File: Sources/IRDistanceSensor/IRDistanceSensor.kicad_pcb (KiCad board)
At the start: 2 copper layers, 31 x 22 mm, 2 parts

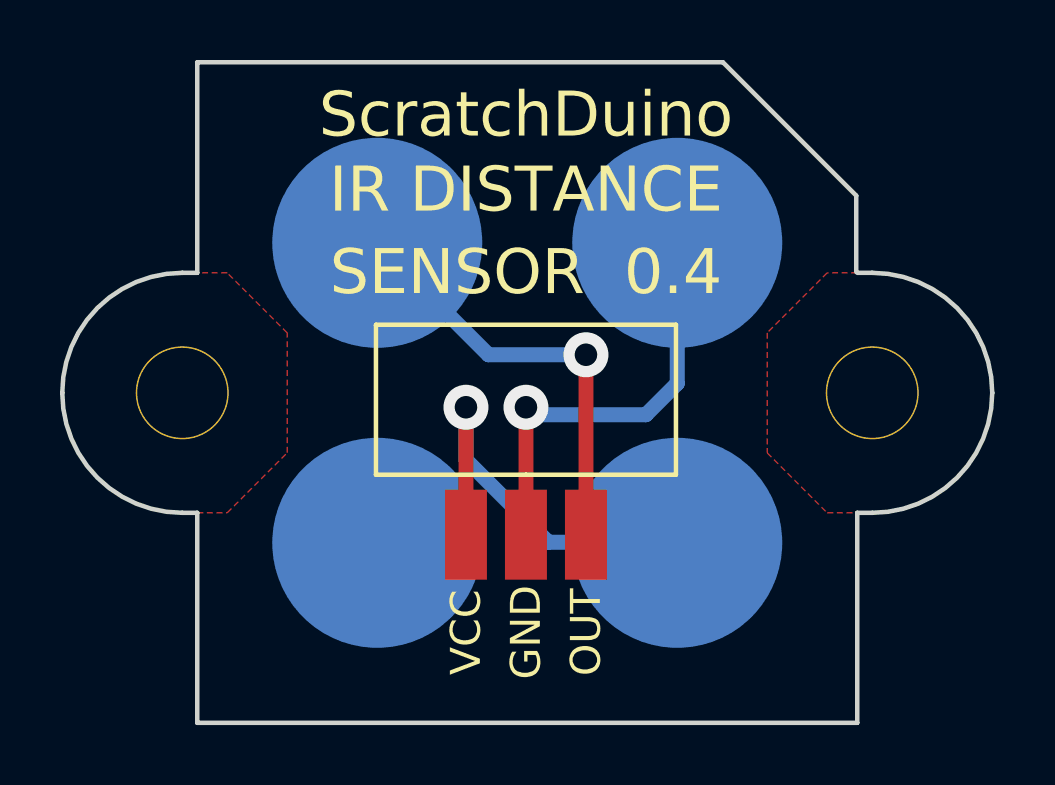
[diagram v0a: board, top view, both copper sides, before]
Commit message: new IR Distance Sensor
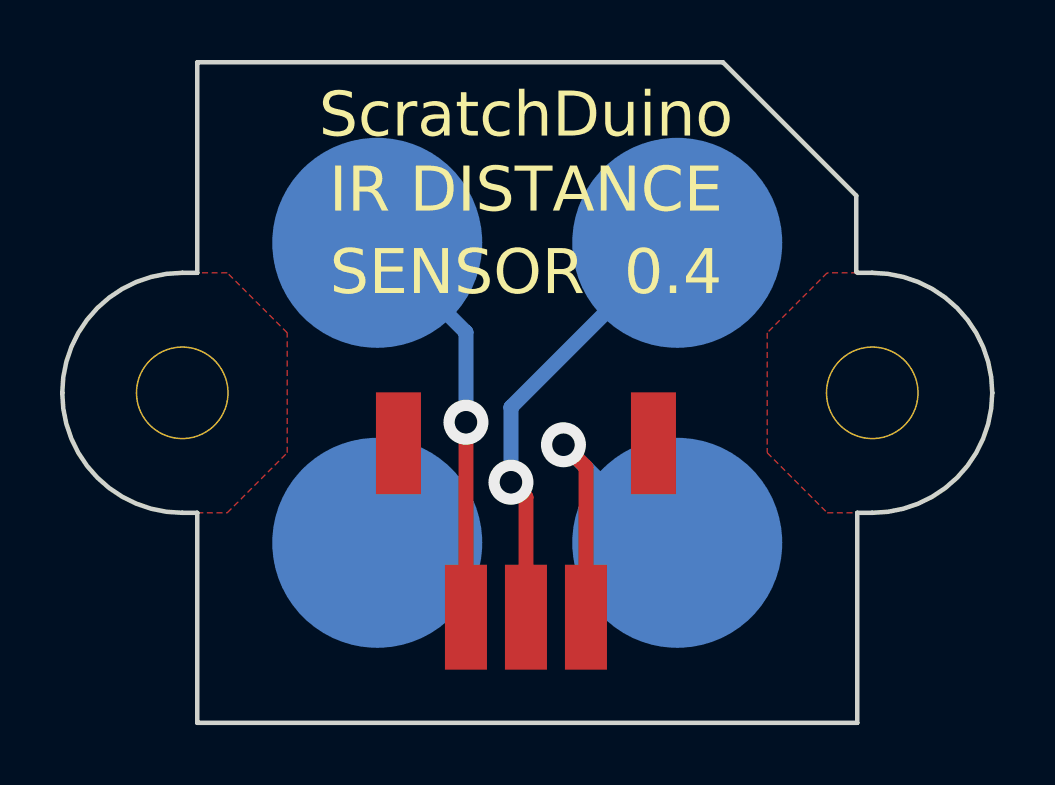
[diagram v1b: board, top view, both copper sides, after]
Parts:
- moved ? 2.75 mm to (29.2, 50.2)
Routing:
- net N-000002: track 14.2 -> 11.2 mm
- net N-000004: track 14.5 -> 13.7 mm
- net N-000003: track 14.5 -> 15.0 mm
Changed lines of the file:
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@@
     (links 3)
     (no_connects 0)
-    (area 13.488999 31.464999 59.829 60.829)
+    (area 13.488999 31.464999 59.829 63.579)
     (thickness 1.6)
     (drawings 18)
-    (tracks 17)
+    (tracks 16)
     (zones 0)
     (modules 2)
@@
     (mod_text_size 1.5 1.5)
     (mod_text_width 0.15)
-    (pad_size 1.4 3)
+    (pad_size 1.5 3.4)
     (pad_drill 0)
     (pad_to_mask_clearance 0.2)
@@
   )
   (module IRDISTANCEWIRE (layer F.Cu)
-    (at 29.25 47.5)
+    (at 29.25 50.25)
     (fp_text reference "" (at 23.5 12.25) (layer F.SilkS)
       (effects (font (size 1.5 1.5) (thickness 0.15)))
@@
       (effects (font (size 1.5 1.5) (thickness 0.15)))
     )
-    (fp_line (start -5 -2) (end -5 -7) (layer F.SilkS) (width 0.15))
-    (fp_line (start -5 -7) (end 5 -7) (layer F.SilkS) (width 0.15))
-    (fp_line (start 5 -7) (end 5 -2) (layer F.SilkS) (width 0.15))
-    (fp_line (start 5 -2) (end 0 -2) (layer F.SilkS) (width 0.15))
-    (fp_line (start 0 -2) (end -5 -2) (layer F.SilkS) (width 0.15))
-    (fp_text user VCC (at -2 3.25 90) (layer F.SilkS)
-      (effects (font (size 1 1) (thickness 0.15)))
-    )
-    (fp_text user GND (at 0 3.25 90) (layer F.SilkS)
-      (effects (font (size 1 1) (thickness 0.15)))
-    )
-    (fp_text user OUT (at 2 3.25 90) (layer F.SilkS)
-      (effects (font (size 1 1) (thickness 0.15)))
-    )
-    (pad 3 smd rect (at 2 0) (size 1.4 3)
+    (pad 5 smd rect (at -4.25 -5.8) (size 1.5 3.4)
+      (layers F.Cu F.Paste F.Mask)
+    )
+    (pad 1 smd rect (at 2 0) (size 1.4 3.5)
+      (layers F.Cu F.Paste F.Mask)
+      (net 1 N-000002)
+    )
+    (pad 2 smd rect (at 0 0) (size 1.4 3.5)
+      (layers F.Cu F.Paste F.Mask)
+      (net 2 N-000003)
+    )
+    (pad 3 smd rect (at -2 0) (size 1.4 3.5)
       (layers F.Cu F.Paste F.Mask)
       (net 3 N-000004)
     )
-    (pad 2 smd rect (at 0 0) (size 1.4 3)
-      (layers F.Cu F.Paste F.Mask)
-      (net 2 N-000003)
-    )
-    (pad 1 smd rect (at -2 0) (size 1.4 3)
-      (layers F.Cu F.Paste F.Mask)
-      (net 1 N-000002)
+    (pad 4 smd rect (at 4.25 -5.8) (size 1.5 3.4)
+      (layers F.Cu F.Paste F.Mask)
     )
   )
@@
   (gr_line (start 18.293 53.769) (end 40.293 53.769) (angle 90) (layer Edge.Cuts) (width 0.15))
   (gr_line (start 18.293 53.769) (end 18.293 46.769) (angle 90) (layer Edge.Cuts) (width 0.15))
-  (segment (start 27.25 47.5) (end 27.25 43.25) (width 0.5) (layer F.Cu) (net 1))
-  (segment (start 34.274 47.75) (end 34.293 47.769) (width 0.5) (layer B.Cu) (net 1))
-  (segment (start 30 47.75) (end 34.274 47.75) (width 0.5) (layer B.Cu) (net 1))
-  (segment (start 27.25 45) (end 30 47.75) (width 0.5) (layer B.Cu) (net 1))
-  (segment (start 27.25 43.25) (end 27.25 45) (width 0.5) (layer B.Cu) (net 1))
-  (via (at 27.25 43.25) (size 1.5) (layers F.Cu B.Cu) (net 1))
-  (segment (start 29.25 47.5) (end 29.25 43.25) (width 0.5) (layer F.Cu) (net 2))
-  (segment (start 34.293 42.457) (end 34.293 37.769) (width 0.5) (layer B.Cu) (net 2))
-  (segment (start 33.25 43.5) (end 34.293 42.457) (width 0.5) (layer B.Cu) (net 2))
-  (segment (start 29.5 43.5) (end 33.25 43.5) (width 0.5) (layer B.Cu) (net 2))
-  (segment (start 29.25 43.25) (end 29.5 43.5) (width 0.5) (layer B.Cu) (net 2))
-  (via (at 29.25 43.25) (size 1.5) (layers F.Cu B.Cu) (net 2))
-  (segment (start 31.25 47.5) (end 31.25 41.5) (width 0.5) (layer F.Cu) (net 3))
-  (segment (start 24.293 37.793) (end 24.293 37.769) (width 0.5) (layer B.Cu) (net 3))
-  (segment (start 28 41.5) (end 24.293 37.793) (width 0.5) (layer B.Cu) (net 3))
-  (segment (start 31.25 41.5) (end 28 41.5) (width 0.5) (layer B.Cu) (net 3))
-  (via (at 31.25 41.5) (size 1.5) (layers F.Cu B.Cu) (net 3))
+  (segment (start 31.25 50.25) (end 31.25 45.25) (width 0.5) (layer F.Cu) (net 1) (status 400000))
+  (segment (start 33.769 47.769) (end 34.293 47.769) (width 0.5) (layer B.Cu) (net 1) (status C00000))
+  (segment (start 30.5 44.5) (end 33.769 47.769) (width 0.5) (layer B.Cu) (net 1) (status 800000))
+  (via (at 30.5 44.5) (size 1.5) (layers F.Cu B.Cu) (net 1))
+  (segment (start 31.25 45.25) (end 30.5 44.5) (width 0.5) (layer F.Cu) (net 1))
+  (segment (start 29.25 50.25) (end 29.25 46.25) (width 0.5) (layer F.Cu) (net 2) (status 400000))
+  (segment (start 34.231 37.769) (end 34.293 37.769) (width 0.5) (layer B.Cu) (net 2) (status C00000))
+  (segment (start 28.75 43.25) (end 34.231 37.769) (width 0.5) (layer B.Cu) (net 2) (status 800000))
+  (segment (start 28.75 45.75) (end 28.75 43.25) (width 0.5) (layer B.Cu) (net 2))
+  (via (at 28.75 45.75) (size 1.5) (layers F.Cu B.Cu) (net 2))
+  (segment (start 29.25 46.25) (end 28.75 45.75) (width 0.5) (layer F.Cu) (net 2))
+  (segment (start 27.25 50.25) (end 27.25 43.75) (width 0.5) (layer F.Cu) (net 3) (status 400000))
+  (segment (start 24.293 37.793) (end 24.293 37.769) (width 0.5) (layer B.Cu) (net 3) (status C00000))
+  (segment (start 27.25 40.75) (end 24.293 37.793) (width 0.5) (layer B.Cu) (net 3) (status 800000))
+  (segment (start 27.25 43.75) (end 27.25 40.75) (width 0.5) (layer B.Cu) (net 3))
+  (via (at 27.25 43.75) (size 1.5) (layers F.Cu B.Cu) (net 3))
   (zone (net 0) (net_name "") (layer F.Cu) (hatch edge 0.508)
     (connect_pads (clearance 1))
